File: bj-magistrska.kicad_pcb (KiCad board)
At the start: 4 copper layers, 75 x 54 mm, 98 parts, among them J1 Screw_Terminal_01x02, J3 Screw_Terminal_01x02, Q1 DMTH10H009LPSQ-13, Q2 BSR14, Q3 PMN280ENEA, SW1 VAL?, SW2 VAL?, SW3 RotaryEncoder_Switch_MP, U1 74LVC1G17, U2 TSV732IS, U3 TSV732IS, U4 NUCLEO144-H743ZI, U5 MCP1501-30xCH

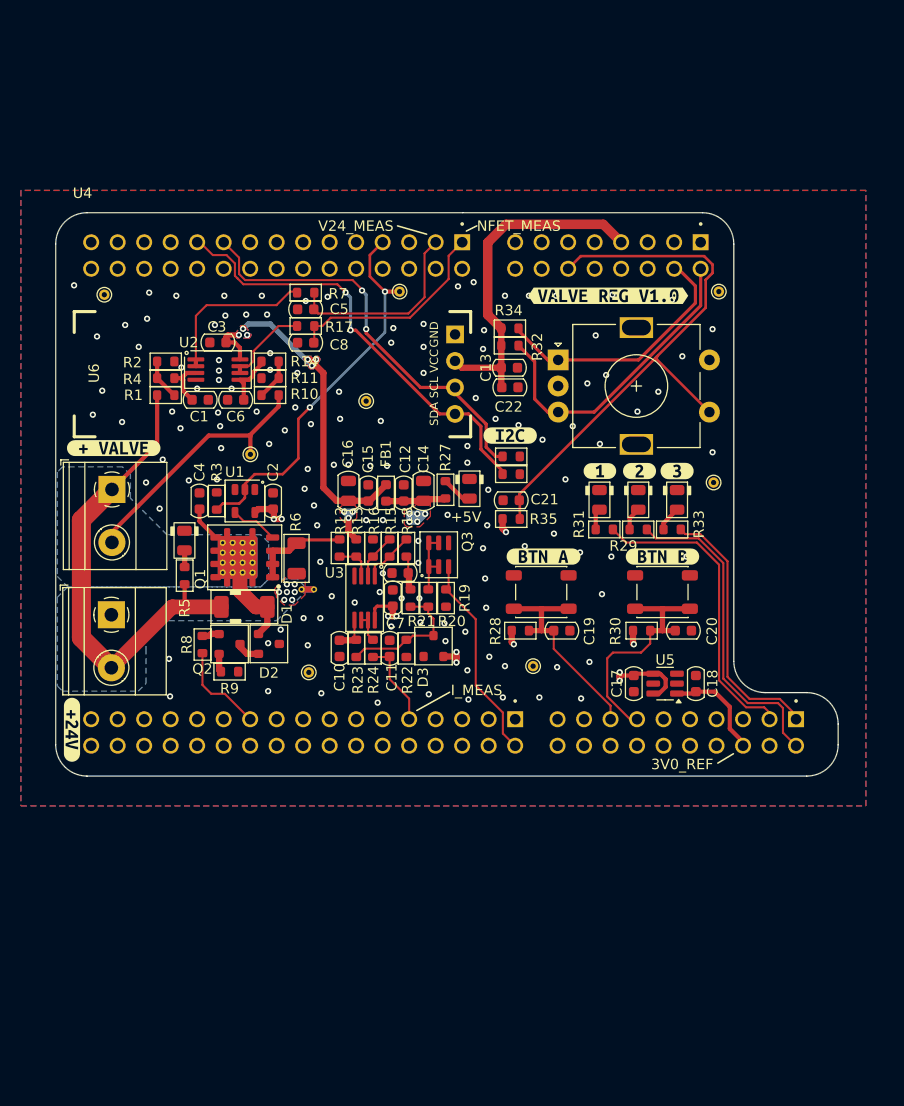
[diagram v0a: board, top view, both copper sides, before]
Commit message: - Removed I2C lines - Added mission resistor between buffer and transistor gate - Removed wetting current & high range enable - Added ILI9341 TFT LCD - Removed OLED - Upped current gain to ~100
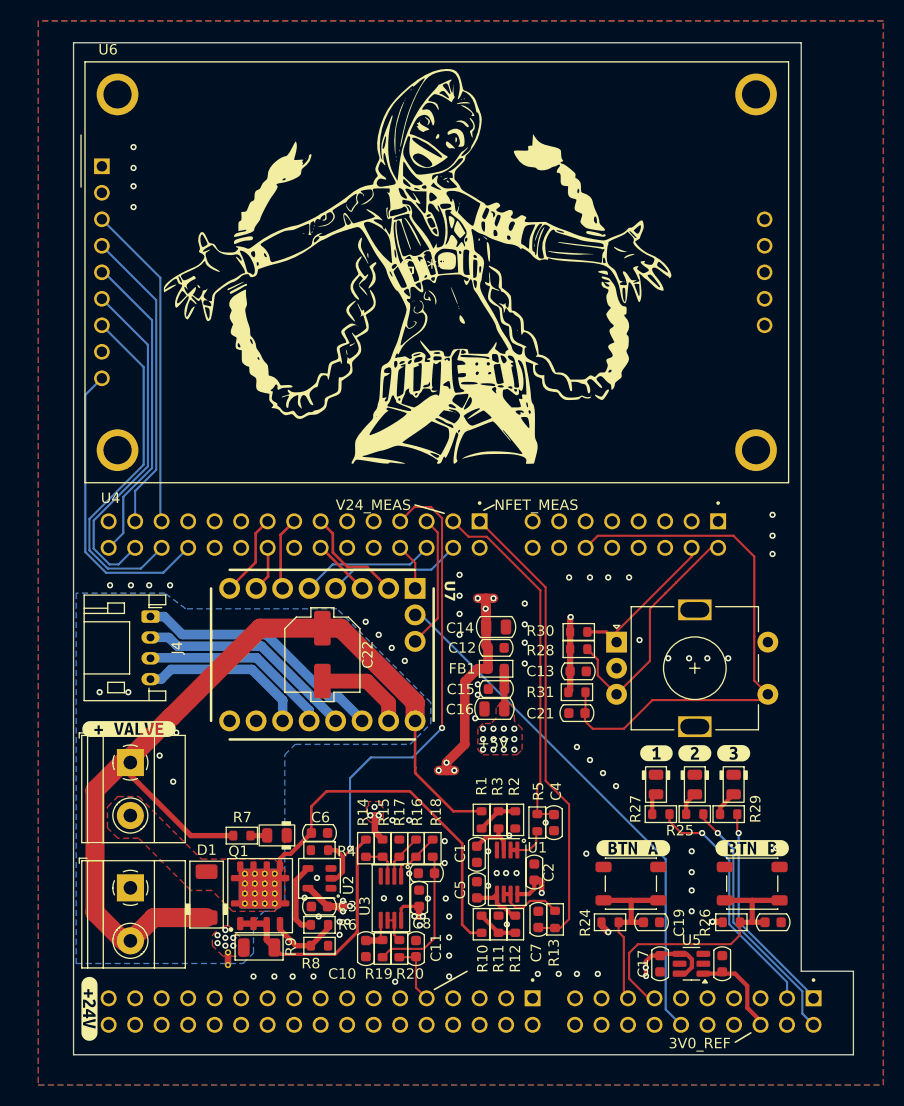
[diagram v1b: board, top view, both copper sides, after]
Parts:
- removed D2: BAV199, PCM_Package_TO_SOT_SMD_AKL:SOT-23
- removed D3: BAT54S, PCM_Package_TO_SOT_SMD_AKL:SOT-23
- removed LED2: LED_0805_Red, PCM_LED_SMD_AKL:LED_0805_2012Metric
- removed Q2: BSR14, PCM_Package_TO_SOT_SMD_AKL:SOT-23
- removed Q3: PMN280ENEA, athanniss-semiconductors:SC-74-6_1.5x2.9mm_P0.95mm
- removed the R19 at (117.5, 104.7)
- removed the R20 at (115.8, 104.7)
- removed R21: 0R, PCM_Resistor_SMD_AKL:R_0603_1608Metric
- removed R22: 100k, PCM_Resistor_SMD_AKL:R_0603_1608Metric
- removed the R25 at (123.8, 91.1)
- removed the R26 at (123.8, 92.8)
- removed the R27 at (117.5, 94.3)
- removed the R9 at (96.8, 111.7)
- removed TP1, TP2: TestPoint, TestPoint:TestPoint_THTPad_D1.0mm_Drill0.5mm
- removed TP3, TP4, TP5, TP6, TP7, TP8: GND, TestPoint:TestPoint_THTPad_D1.0mm_Drill0.5mm
- removed kibuzzard-66E6F41C: G***, kibuzzard-66E6F41C
- removed kibuzzard-66E6F432: G***, kibuzzard-66E6F432
- added G***: LOGO, LOGO, F.Cu at (115.4, 73.0)
- added J4: Conn_01x04, Connector_JST:JST_PH_S4B-PH-K_1x04_P2.00mm_Horizontal, F.Cu at (89.2, 106.5)
- added R6: 1k, PCM_Resistor_SMD_AKL:R_0603_1608Metric, F.Cu at (105.4, 136.0)
- added U7: ~, athaniss-device:BTT-TMC2209-V1.3_RAISED, F.Cu at (105.7, 110.1)
- C22: value 100n -> 100 uF; footprint PCM_Capacitor_SMD_AKL:C_0603_1608Metric -> PCM_Capacitor_SMD_AKL:C_Elec_6.3x7.7
- R16: renamed from R15; value 56k -> 180k
- R8: value 4k7 -> 47k
- U6: value ~ -> CR2013-MI2120; footprint athanniss-lcd:SSD1306-0.91-OLED-4pin-128x32_no-header-offset -> Display:CR2013-MI2120
- moved R13 61.7 mm to (128.0, 135.5), turned to -90 degrees
- moved C7 59.6 mm to (126.4, 135.5), turned to 90 degrees
- moved C2 59.1 mm to (126.0, 130.9), turned to 90 degrees
- moved R12 58.8 mm to (124.2, 135.9), turned to 90 degrees
- moved R11 56.7 mm to (122.6, 135.9), turned to 90 degrees
- moved U1 55.6 mm to (123.4, 130.9), turned to -90 degrees
- moved R5 55.4 mm to (126.3, 126.2), turned to 90 degrees
- moved R2 55.3 mm to (124.2, 125.9), turned to -90 degrees
- moved C4 54.7 mm to (127.9, 126.2), turned to -90 degrees
- moved R10 54.6 mm to (121.0, 135.9), turned to 90 degrees
- moved R3 53.0 mm to (122.6, 125.9), turned to -90 degrees
- moved C5 52.3 mm to (120.5, 132.6), turned to 90 degrees
- moved C1 51.0 mm to (120.5, 129.2), turned to -90 degrees
- moved R1 50.7 mm to (121.0, 125.9), turned to -90 degrees
- moved C3 39.1 mm to (105.4, 134.2), turned to 180 degrees
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- renumbered C3 to C2, C2 to C3, C5 to C4, C6 to C5, C4 to C6, C8 to C7, C7 to C8, R14 to R12, R17 to R13, R12 to R14, R13 to R15, R16 to R17, R23 to R19, R24 to R20, R28 to R24, R29 to R25, R30 to R26, R31 to R27, R32 to R28, R33 to R29, R4 to R3, R34 to R30, R35 to R31, R3 to R4, R7 to R5, R5 to R7, R6 to R9, U2 to U1, U1 to U2
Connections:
- C22 pad 1: +3V3 -> +12V
- C22 pad 2: GND -> GNDPWR
- D1 pad 1: /Output_Analog/LS1_OUT -> +12V
- J1 pad 1: /Output_Analog/PWR_GND -> GNDPWR
- J1 pad 2: /Output_Analog/LS1_OUT -> +12V
- J3 pad 1: /Output_Analog/LS1_OUT -> +12V
- NT1 pad 2: /Output_Analog/PWR_GND -> GNDPWR
- R1 pad 1: /Output_Analog/LS1_OUT -> +12V
- R19 pad 1: Net-(D3-C) -> Net-(C9-Pad1)
- R7 pad 1: /Output_Analog/LS1_OUT -> +12V
- R8 pad 1: /Nucleo-144/EN_WETTING_CURRENT -> GND
- R8 pad 2: Net-(Q2-B) -> Net-(Q1-PadG)
- R9 pad 2: /Output_Analog/PWR_GND -> GNDPWR
- U2 pad 4: Net-(Q1-PadG) -> Net-(R6-Pad1)
- U4 pad CN10_2: /Nucleo-144/E_HIGH_I_RANGE -> unconnected-(U4-PG12-PadCN10_2)
- U4 pad CN10_21: /Nucleo-144/EN_WETTING_CURRENT -> unconnected-(U4-PD12-PadCN10_21)
- U4 pad CN7_12: unconnected-(U4-PA6-PadCN7_12) -> TMC2209_VREF
- U4 pad CN9_13: unconnected-(U4-РВ2-PadCN9_13) -> TMC2209_MS1
- U4 pad CN9_14: unconnected-(U4-PE2-PadCN9_14) -> TMC2209_MS2
- U4 pad CN9_15: unconnected-(U4-РЕ9-PadCN9_15) -> TMC2209_CLK
- U4 pad CN9_17: unconnected-(U4-PF2-PadCN9_17) -> TMC2209_DIR
- U4 pad CN9_18: unconnected-(U4-РЕ5-PadCN9_18) -> TMC2209_STEP
- U4 pad CN9_19: /Nucleo-144/I2C_SCK -> unconnected-(U4-PF1-PadCN9_19)
- U4 pad CN9_21: /Nucleo-144/I2C_SDA -> unconnected-(U4-PF0-PadCN9_21)
- U4 pad CN9_24: unconnected-(U4-PF8-PadCN9_24) -> ILI9341_SPI_MISO
- U4 pad CN9_25: unconnected-(U4-PD0-PadCN9_25) -> ILI9341_SPI_CS
- U4 pad CN9_26: unconnected-(U4-PF7-PadCN9_26) -> ILI9341_SPI_SCK
- U4 pad CN9_27: unconnected-(U4-PD1-PadCN9_27) -> ILI9341_RESET
- U4 pad CN9_28: unconnected-(U4-PF9-PadCN9_28) -> ILI9341_SPI_MOSI
- U4 pad CN9_30: unconnected-(U4-PG1-PadCN9_30) -> ILI9341_SPI_DC
- U4 pad CN9_4: unconnected-(U4-PD6-PadCN9_4) -> TMC2209_RX
- U4 pad CN9_5: unconnected-(U4-РСЗ-PadCN9_5) -> TMC2209_DIAG
- U4 pad CN9_6: unconnected-(U4-PD5-PadCN9_6) -> TMC2209_TX
- U4 pad CN9_8: unconnected-(U4-PD4-PadCN9_8) -> TMC2209_EN
- U6 pad 1: GND -> +3V3
- U6 pad 2: +3V3 -> GND
- U6 pad 3: /Nucleo-144/I2C_SCK -> ILI9341_SPI_CS
- U6 pad 4: /Nucleo-144/I2C_SDA -> ILI9341_RESET
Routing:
- net +12V: track 0.00 -> 93.1 mm
- net +3V3: track 78.8 -> 9.51 mm
- net +5VA: track 90.3 -> 26.5 mm, vias 13 -> 20
- net TMC2209_VREF: track 0.00 -> 50.2 mm
- net /Output_Analog/LS1_OUT: track 45.5 -> 0.00 mm
- net /Nucleo-144/I2C_SDA: track 43.0 -> 0.00 mm, vias 2 -> 0
- net /Nucleo-144/I2C_SCK: track 40.0 -> 0.00 mm, vias 2 -> 0
- net ILI9341_SPI_SCK: track 0.00 -> 33.8 mm
- net ILI9341_SPI_MOSI: track 0.00 -> 33.2 mm
- net ILI9341_SPI_CS: track 0.00 -> 31.3 mm
- net ILI9341_SPI_DC: track 0.00 -> 30.2 mm
- net ILI9341_RESET: track 0.00 -> 29.4 mm
- net ILI9341_SPI_MISO: track 0.00 -> 29.0 mm
- net /Nucleo-144/V_NFET_MEAS: track 20.4 -> 45.0 mm
- net Net-(J4-Pin_1): track 0.00 -> 24.4 mm
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- added copper zone on In2.Cu, net +3V3
- added copper zone on In2.Cu, net +5VA
- added copper zone on F.Cu, net /Output_Analog/LS1_RETURN
- added copper zone on B.Cu, net GNDPWR
- added copper zone on F.Cu, net GNDPWR
- removed copper zone on B.Cu, net +5VA
- removed copper zone on F.Cu, net +5VD
- removed copper zone on In2.Cu, net +5VD
- removed copper zone on B.Cu, net /Output_Analog/LS1_RETURN
- removed copper zone on B.Cu, net /Output_Analog/PWR_GND
- removed copper zone on F.Cu, net /Output_Analog/PWR_GND
- removed copper zone on In2.Cu, net GND
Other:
- board size 75 x 54 mm -> 74.8 x 97 mm
- board text removed: "I_MEAS"

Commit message: JINX V2.0
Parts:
- added G***: LOGO, LOGO, F.Cu at (100.6, 61.2)
- added G***: LOGO, LOGO, F.Cu at (140.5, 59.3)
- added G***: LOGO, LOGO, F.Cu at (97.6, 87.0)
- moved G*** 7.59 mm to (122.8, 74.7)
- moved kibuzzard-66E6F4F3 1.95 mm to (83.3, 142.1)
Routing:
- net Net-(J4-Pin_3): track 18.3 -> 18.9 mm
- net Net-(J4-Pin_4): track 16.2 -> 16.8 mm
- net Net-(J4-Pin_2): track 21.0 -> 21.6 mm
- net GNDPWR: track 8.97 -> 8.43 mm, vias 7 -> 33
- net GND: vias 87 -> 106
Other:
- outline, holes or cut-outs redrawn
- board text added: "J4"
